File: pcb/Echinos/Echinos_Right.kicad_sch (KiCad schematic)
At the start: 0 parts

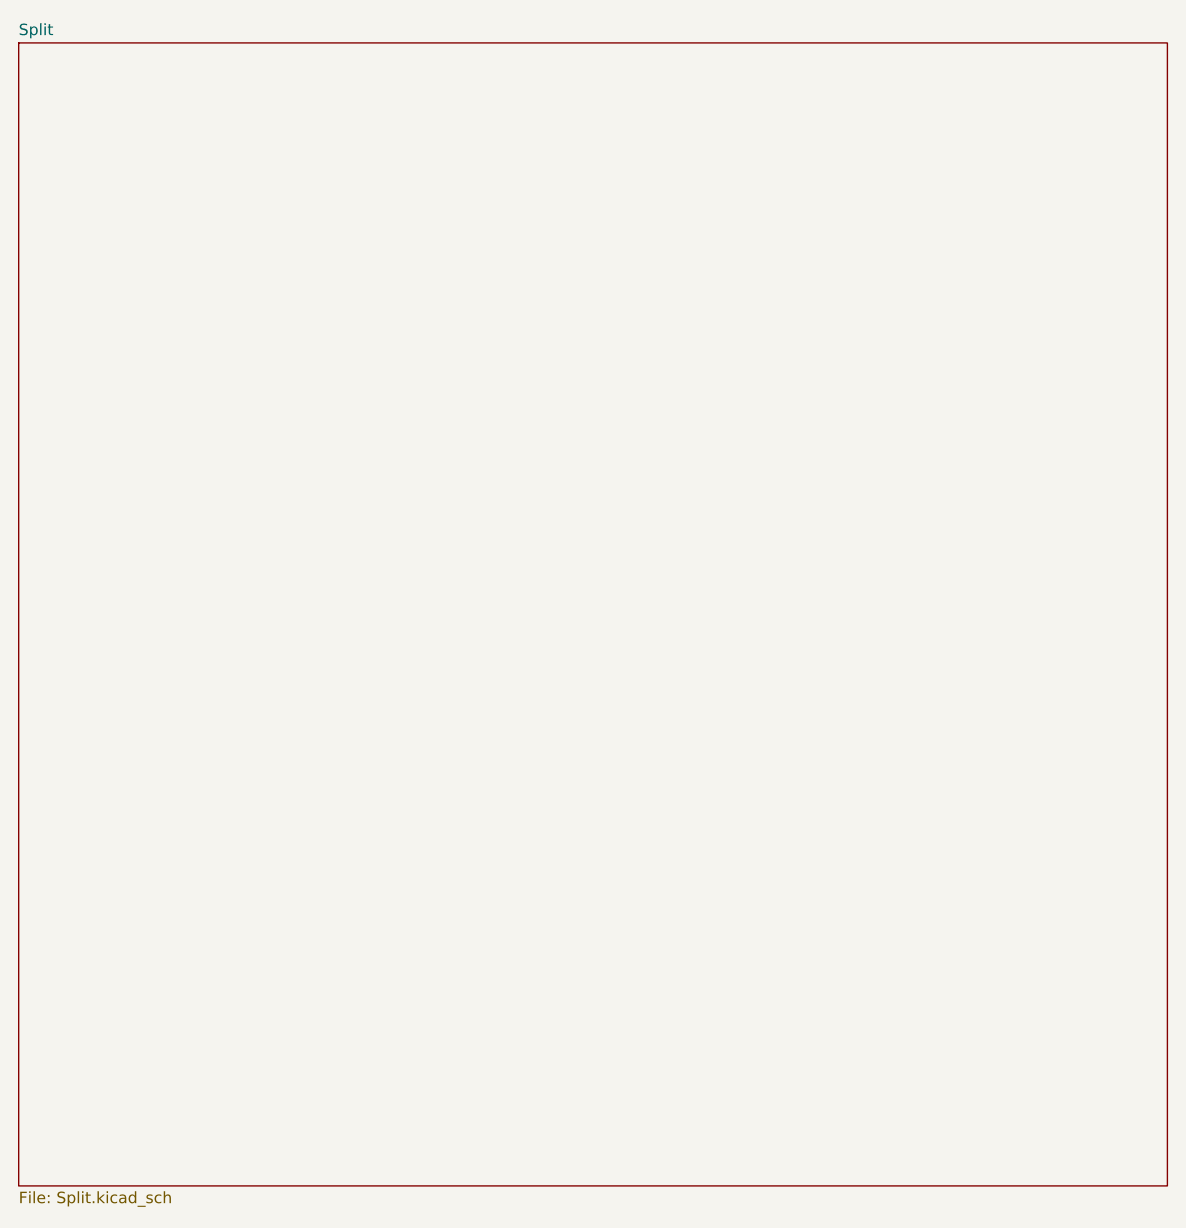
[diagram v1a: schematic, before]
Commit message: 💥 [PCB] - Split schematic for left and right halves.   - Required to create a common PCB to lower the manufacturing cost
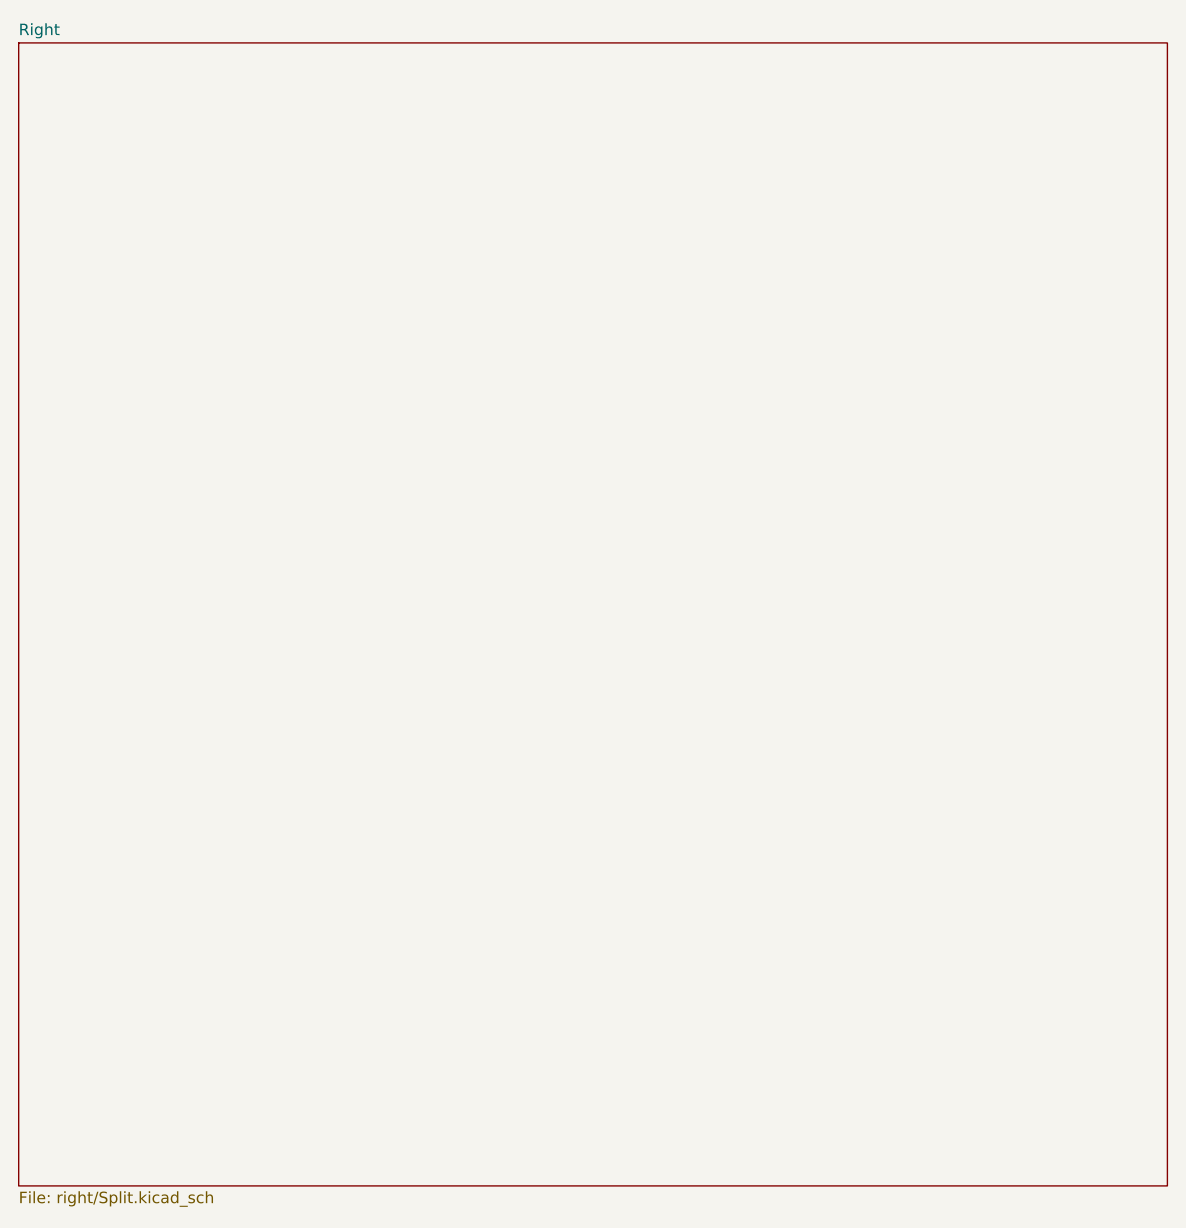
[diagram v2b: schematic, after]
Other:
- sheet Split renamed Right
- sheet Right: file Split.kicad_sch -> right/Split.kicad_sch
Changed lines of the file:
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@@
 			(color 0 0 0 0)
 		)
-		(property "Sheetname" "Split"
+		(property "Sheetname" "Right"
 			(at 63.5 62.1534 0)
 			(show_name no)
@@
 			)
 		)
-		(property "Sheetfile" "Split.kicad_sch"
+		(property "Sheetfile" "right/Split.kicad_sch"
 			(at 63.5 190.4496 0)
 			(show_name no)
